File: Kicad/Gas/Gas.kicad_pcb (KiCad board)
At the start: 2 copper layers, 9 parts, among them J1 MG811, J2 Arduino, J3 MQ135

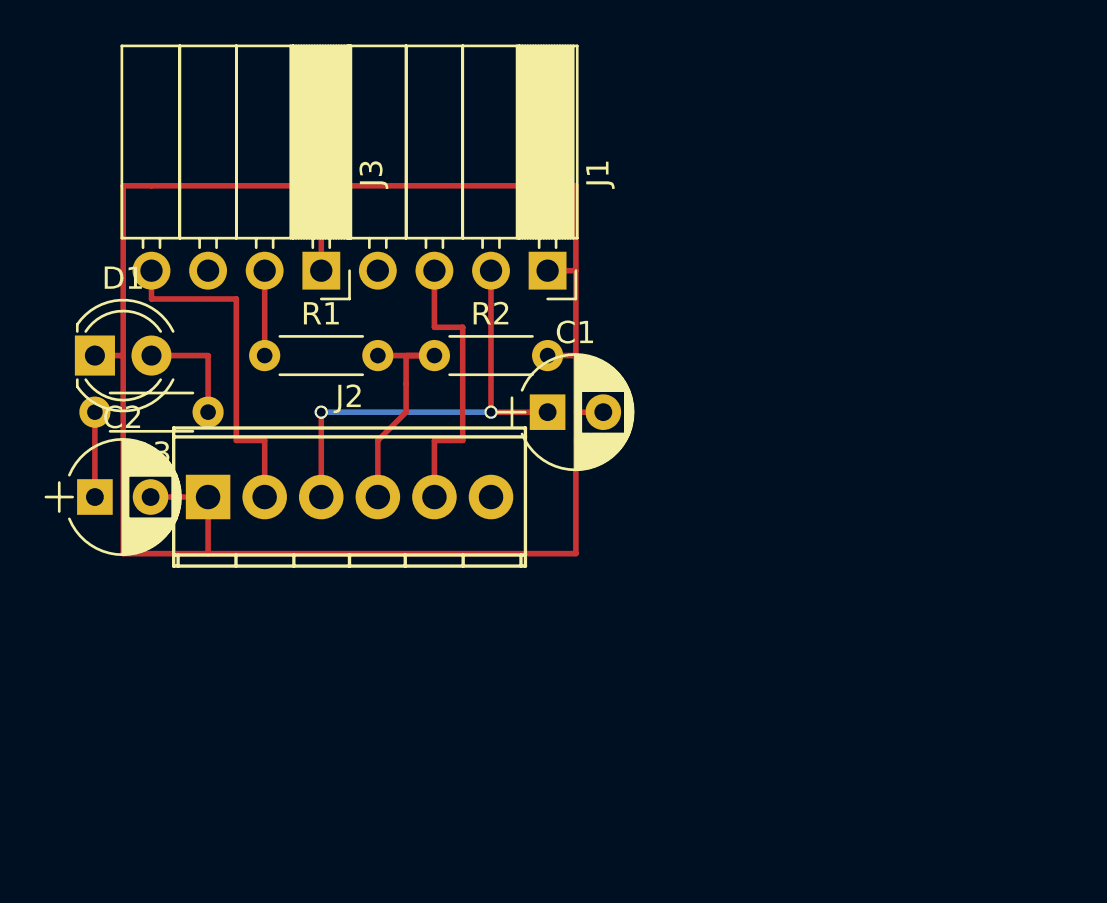
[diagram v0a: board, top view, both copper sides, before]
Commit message: Added air quality sensor to Kicad Gas schematic. Added code for CCS811. Note: arduino program is temporarily not compiling.
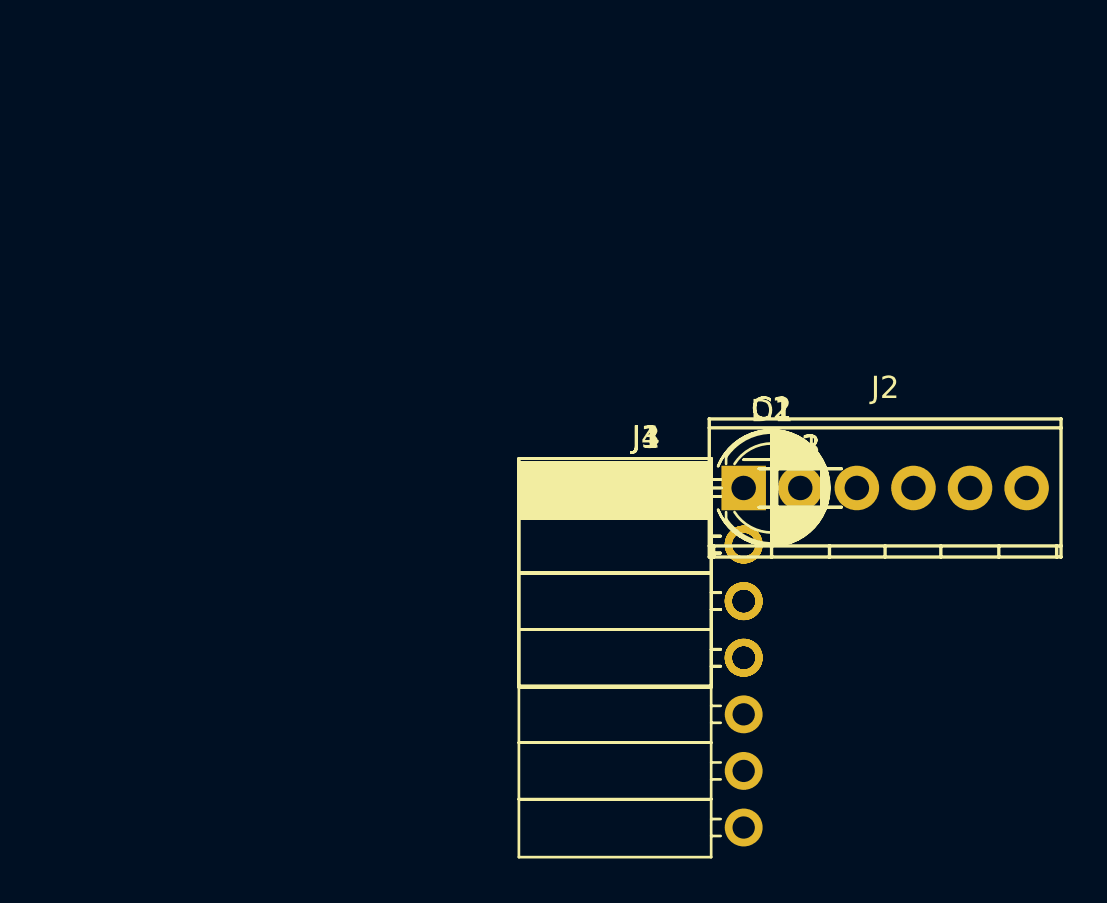
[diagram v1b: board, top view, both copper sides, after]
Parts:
- added J4: CCS811, Socket_Strips:Socket_Strip_Angled_1x07_Pitch2.54mm, F.Cu at (148.5, 105.0)
- moved D1 29.7 mm to (148.5, 105.0)
- moved C2 29.1 mm to (148.5, 105.0)
- moved R3 24.3 mm to (148.5, 105.0), turned to 0 degrees
- moved J2 24.0 mm to (148.5, 105.0)
- moved R1 22.3 mm to (148.5, 105.0)
- moved J3 21.3 mm to (148.5, 105.0), turned to 0 degrees
- moved R2 15.1 mm to (148.5, 105.0)
- moved J1 13.1 mm to (148.5, 105.0), turned to 0 degrees
- moved C1 9.44 mm to (148.5, 105.0)
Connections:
- J1 pad 3: Net-(J1-Pad3) -> (no net)
- J2 pad 3: +5V -> Vout
- J2 pad 4: Vout -> /SDA
- J2 pad 5: Net-(J1-Pad3) -> /SCL
- J2 pad 6: (no net) -> /nWAKE
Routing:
- net GND: track 87.6 -> 0.00 mm
- net +5V: track 20.3 -> 0.00 mm, vias 2 -> 0
- net +3V3: track 19.0 -> 0.00 mm
- net Net-(J1-Pad3): track 12.7 -> 0.00 mm
- net Vout: track 10.7 -> 0.00 mm
- net Net-(D1-Pad2): track 5.08 -> 0.00 mm
- net Vin: track 3.81 -> 0.00 mm

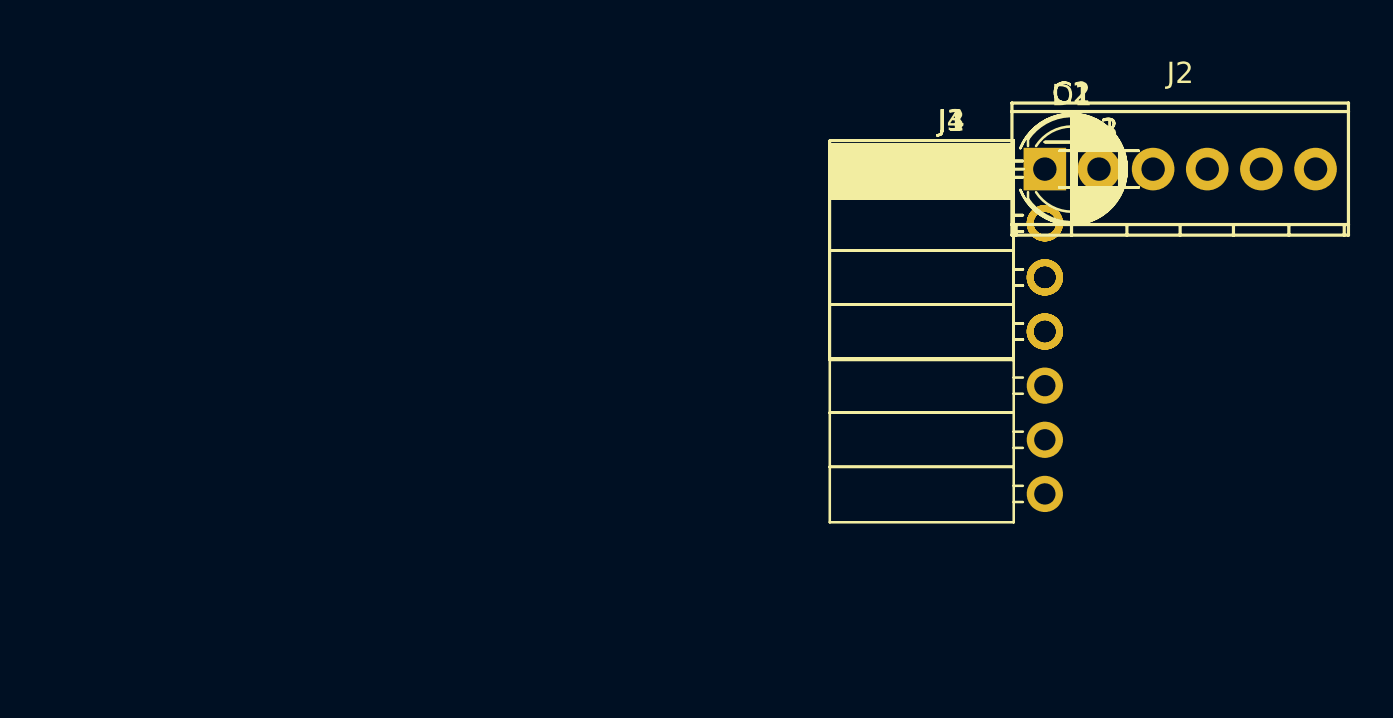
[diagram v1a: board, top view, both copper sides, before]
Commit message: Added RTC. RTC integration with SD file paths and log files. Added time tag to data log.
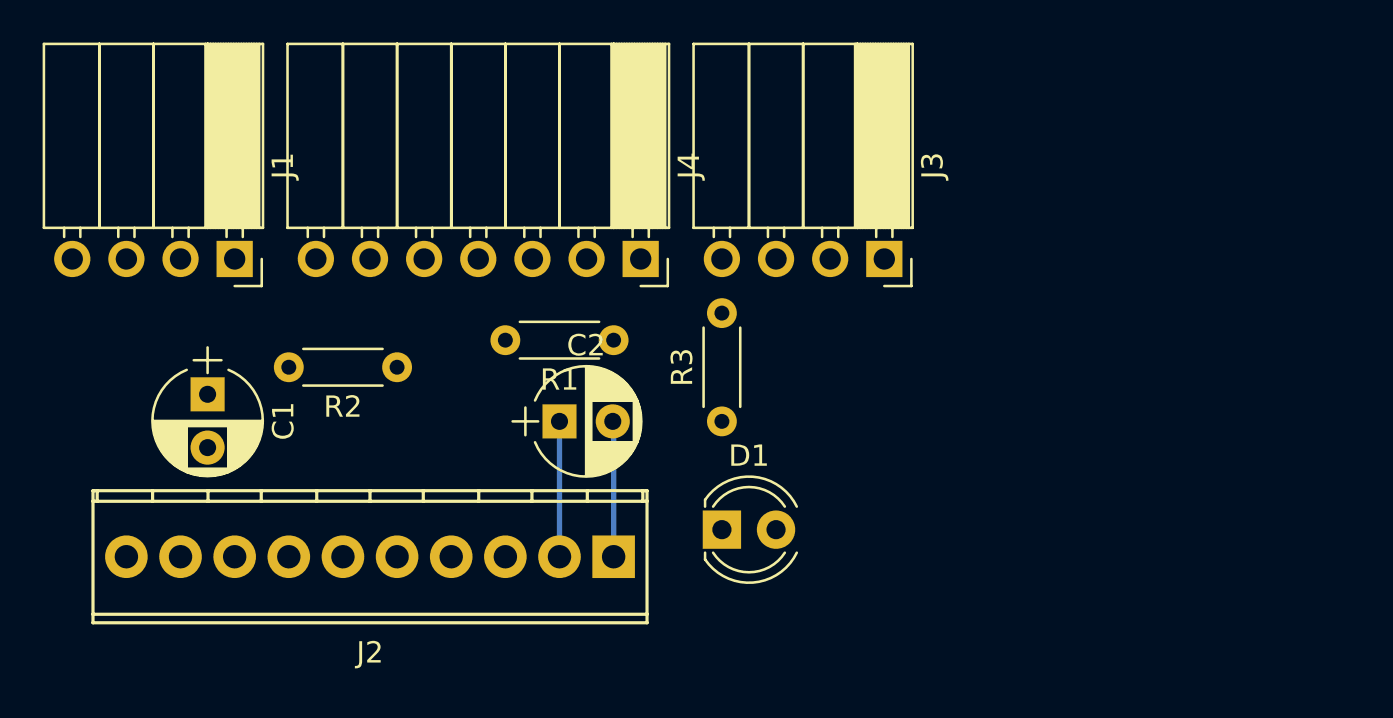
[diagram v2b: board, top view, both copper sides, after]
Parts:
- J2: footprint Connectors_Terminal_Blocks:TerminalBlock_Pheonix_MPT-2.54mm_6pol -> Connectors_Terminal_Blocks:TerminalBlock_Pheonix_MPT-2.54mm_10pol
- moved C1 40.7 mm to (109.2, 115.6), turned to 270 degrees
- moved J1 38.2 mm to (110.5, 109.2), turned to 270 degrees
- moved R2 31.8 mm to (118.1, 114.3), turned to 180 degrees
- moved J2 27.2 mm to (128.3, 123.2), turned to 180 degrees
- moved C2 25.7 mm to (125.7, 116.8)
- moved D1 22.7 mm to (133.3, 121.9)
- moved R1 21.8 mm to (128.3, 113.0), turned to 180 degrees
- moved J4 19.4 mm to (129.5, 109.2), turned to 270 degrees
- moved R3 19.2 mm to (133.3, 116.8), turned to 90 degrees
- moved J3 8.63 mm to (141.0, 109.2), turned to 270 degrees
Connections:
- J1 pad 3: (no net) -> Net-(J1-Pad3)
- J4 pad 6: (no net) -> /nINT
- J4 pad 7: (no net) -> /nRST
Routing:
- net GND: track 0.00 -> 6.37 mm
- net +3V3: track 0.00 -> 6.35 mm

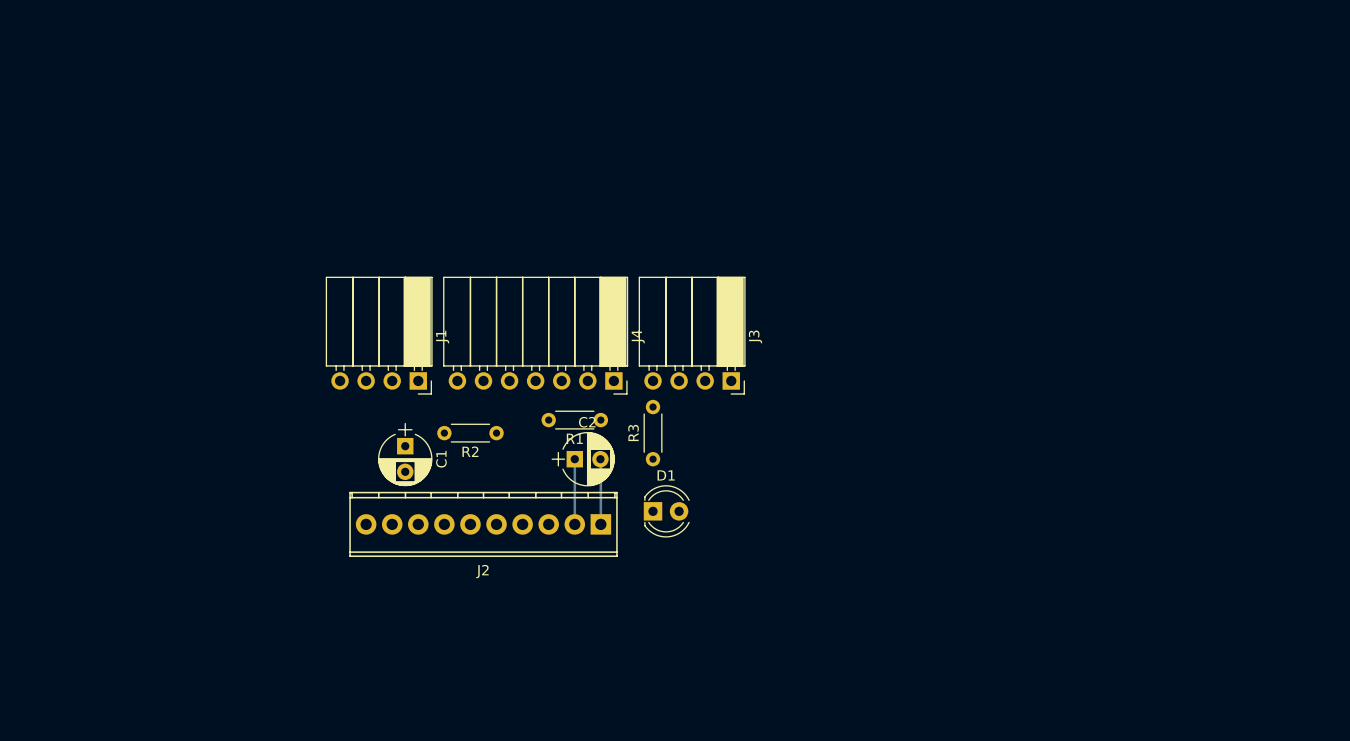
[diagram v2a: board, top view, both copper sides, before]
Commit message: Added PH4 connectors libs; Finshed CO2 sensors schematic circuit.
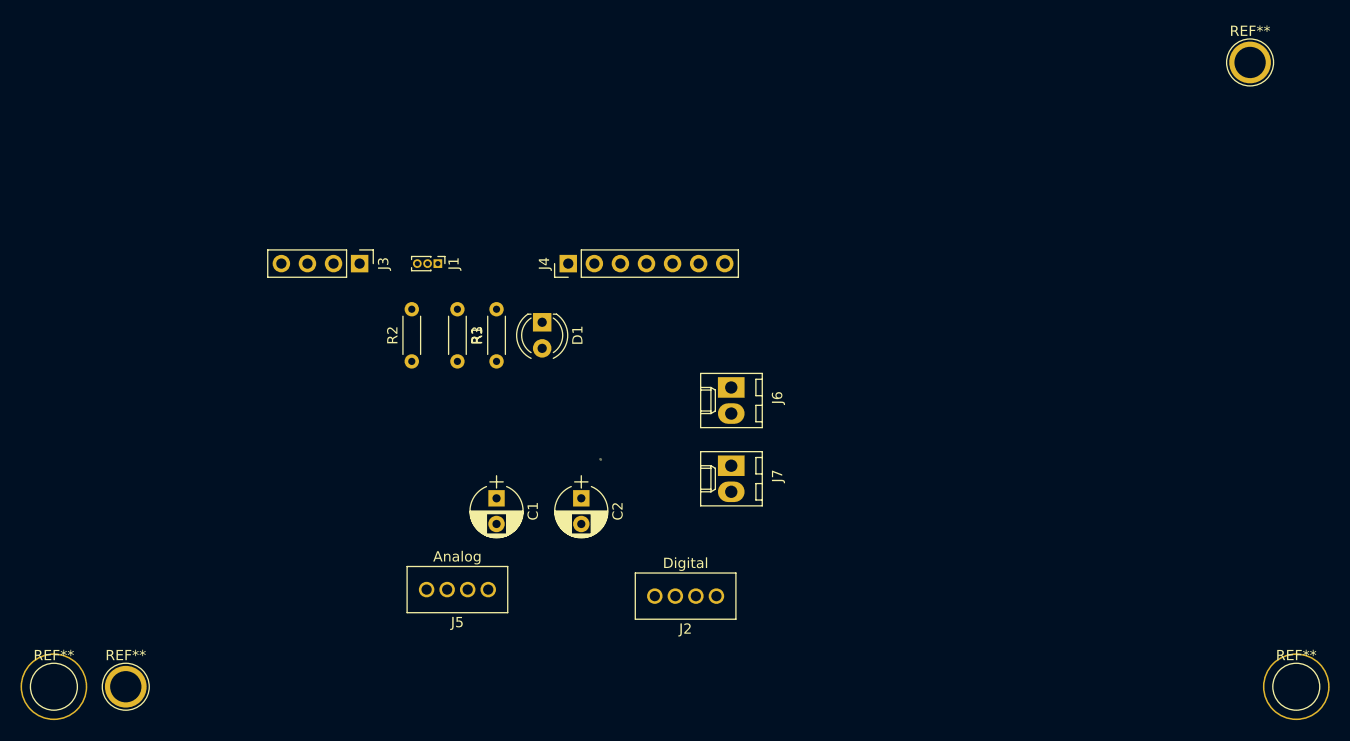
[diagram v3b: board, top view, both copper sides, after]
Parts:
- added J5: Analog, ecoPlanos_custom:JST_PHR-4, F.Cu at (114.3, 129.5)
- added J6: CONN_01X02, Connectors_Molex:Molex_KK-6410-02_02x2.54mm_Straight, F.Cu at (141.0, 109.9)
- added J7: CONN_01X02, Connectors_Molex:Molex_KK-6410-02_02x2.54mm_Straight, F.Cu at (141.0, 117.5)
- added REF**: 1pin, Connectors:1pin, F.Cu at (196.0, 139.0)
- added REF**: 1pin, Connectors:1pin, F.Cu at (191.5, 78.2)
- added REF**: 1pin, Connectors:1pin, F.Cu at (82.0, 139.0)
- added REF**: 1pin, Connectors:1pin, F.Cu at (75.0, 139.0)
- J1: footprint Socket_Strips:Socket_Strip_Angled_1x04_Pitch2.54mm -> Pin_Headers:Pin_Header_Straight_1x03_Pitch1.00mm
- J2: value Arduino -> Digital; footprint Connectors_Terminal_Blocks:TerminalBlock_Pheonix_MPT-2.54mm_10pol -> ecoPlanos_custom:JST_PHR-4
- J3: footprint Socket_Strips:Socket_Strip_Angled_1x04_Pitch2.54mm -> Pin_Headers:Pin_Header_Straight_1x04_Pitch2.54mm
- J4: footprint Socket_Strips:Socket_Strip_Angled_1x07_Pitch2.54mm -> Pin_Headers:Pin_Header_Straight_1x07_Pitch2.54mm
- moved J3 38.0 mm to (104.8, 97.8)
- moved D1 21.3 mm to (122.6, 103.5), turned to 270 degrees
- moved R3 18.0 mm to (118.1, 107.3)
- moved R1 17.7 mm to (114.3, 102.2), turned to 270 degrees
- moved J4 12.3 mm to (125.1, 97.8), turned to 90 degrees
- moved J1 11.6 mm to (112.4, 97.8)
- moved J2 10.8 mm to (136.5, 130.2)
- moved R2 10.8 mm to (109.9, 107.3), turned to 90 degrees
- moved C1 10.2 mm to (118.1, 120.7)
- moved C2 3.86 mm to (126.4, 120.7), turned to 270 degrees
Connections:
- net Vin renamed Net-(J3-Pad2)
- C1 pad 1: +5V -> +3V3
- C2 pad 1: +3V3 -> +5V
- J1 pad 2: +5V -> +3V3
- J2 pad 1: GND -> (no net)
- J2 pad 2: +3V3 -> /nRST
- J2 pad 3: Vout -> /nINT
- J2 pad 4: /SDA -> /nWAKE
- J3 pad 4: +3V3 -> +5V
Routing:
- net GND: track 6.37 -> 0.00 mm
- net +3V3: track 6.35 -> 0.00 mm
